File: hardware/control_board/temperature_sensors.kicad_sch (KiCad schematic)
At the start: 24 parts, among them J5 RTD, J5 TC, U2 MAX6675, U5 MCP6N11T-005E, U7 MCP6001T

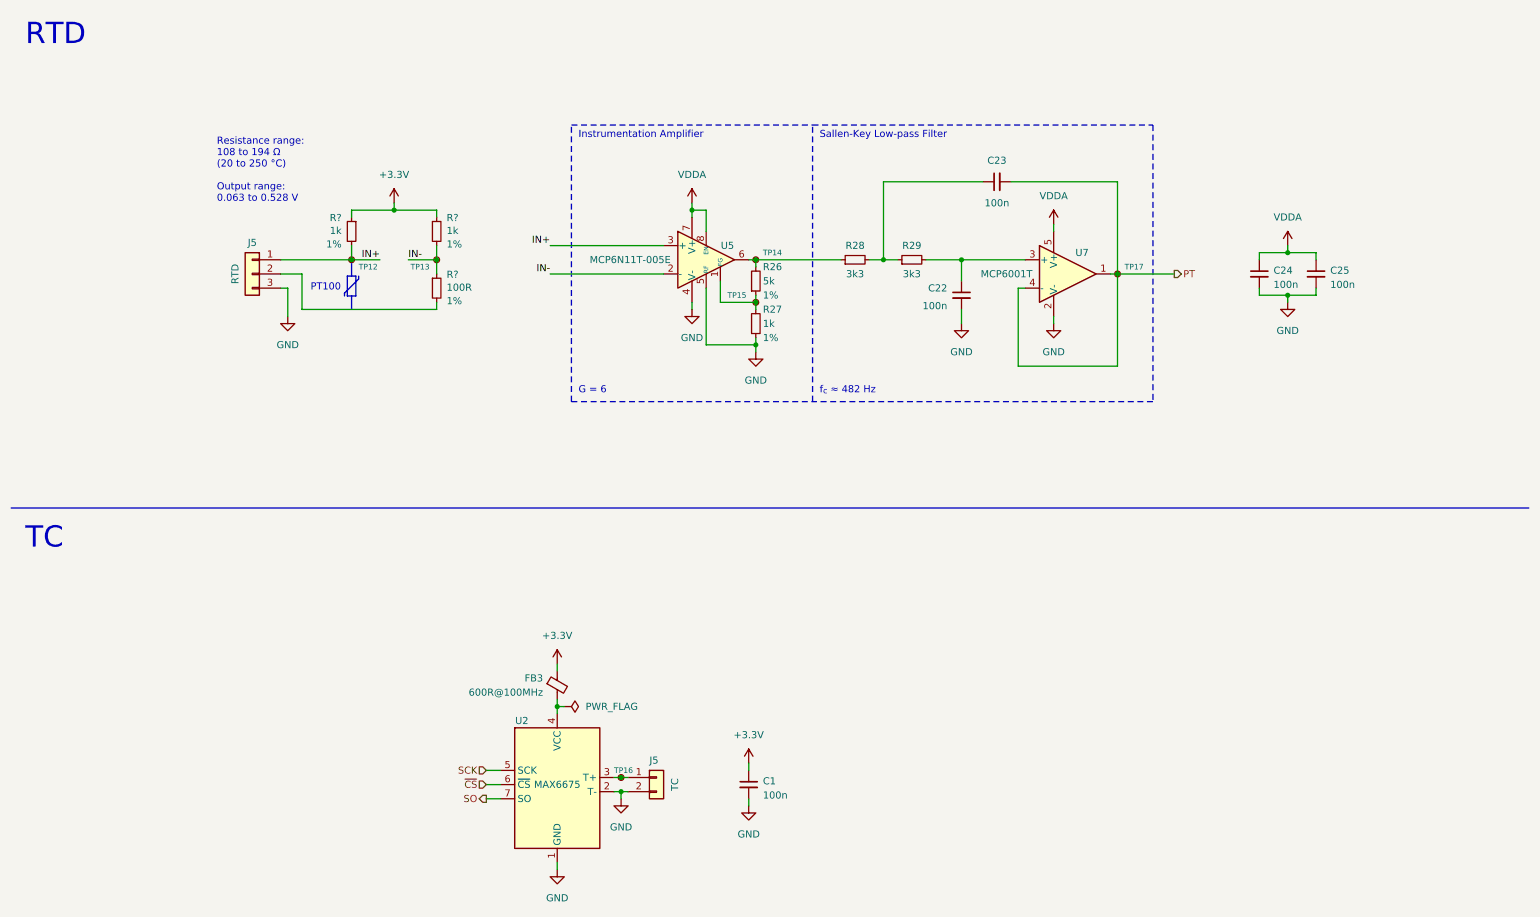
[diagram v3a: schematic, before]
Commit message: Place components on the control board PCB
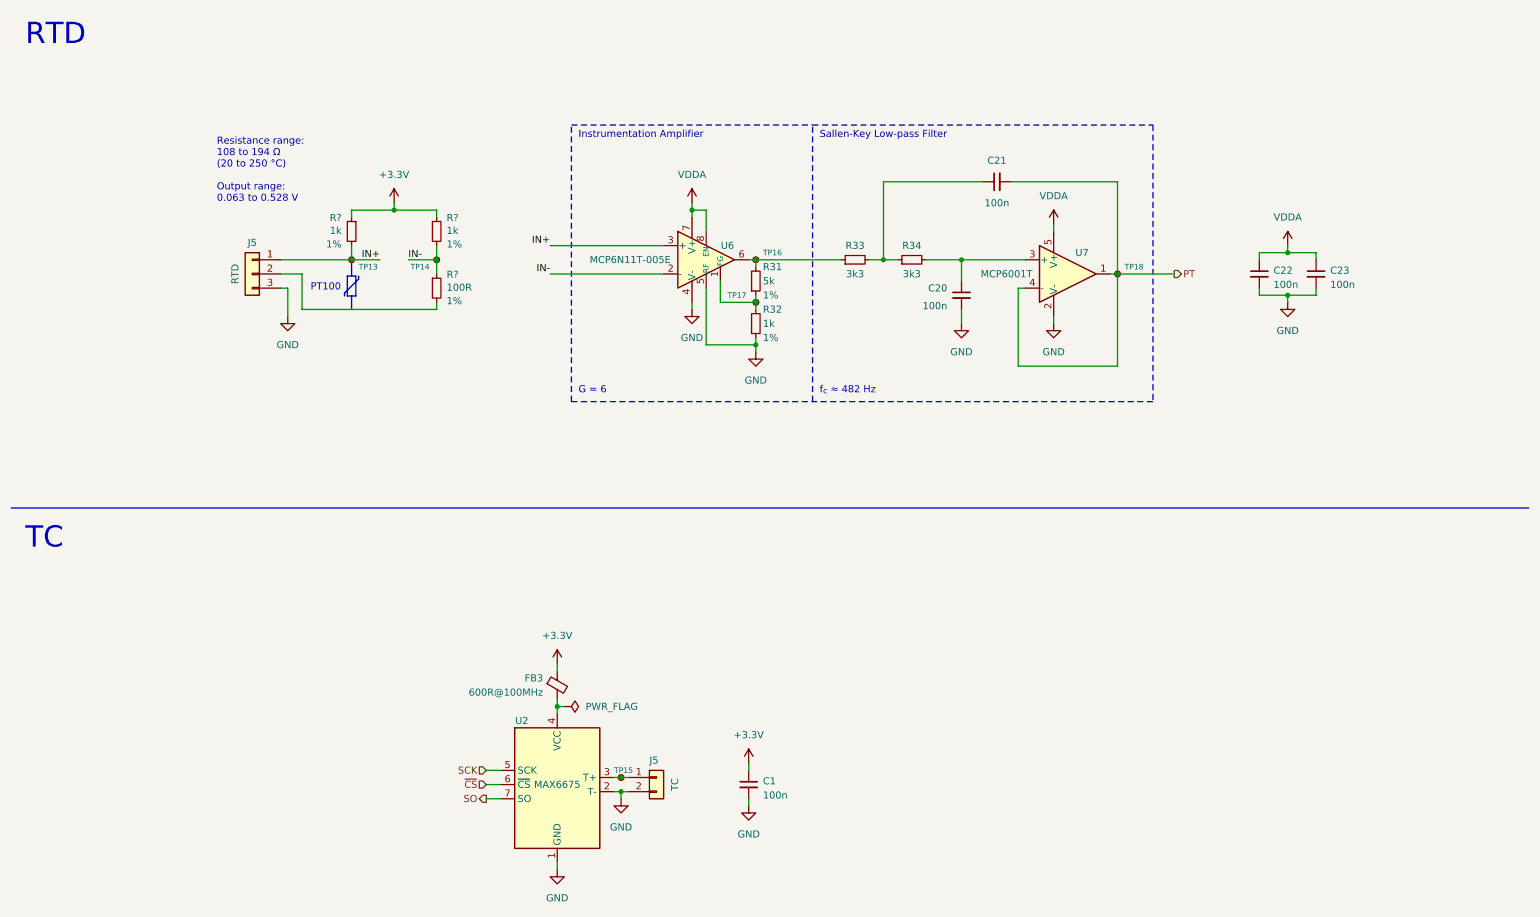
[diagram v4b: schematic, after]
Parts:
- renumbered C22 to C20, C23 to C21, C24 to C22, C25 to C23, R26 to R31, R27 to R32, R28 to R33, R29 to R34, TP12 to TP13, TP13 to TP14, TP16 to TP15, TP14 to TP16, TP15 to TP17, TP17 to TP18, U5 to U6
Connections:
- net GND: no longer U6.9 (EP)

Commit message: Route front panel PCB tracks
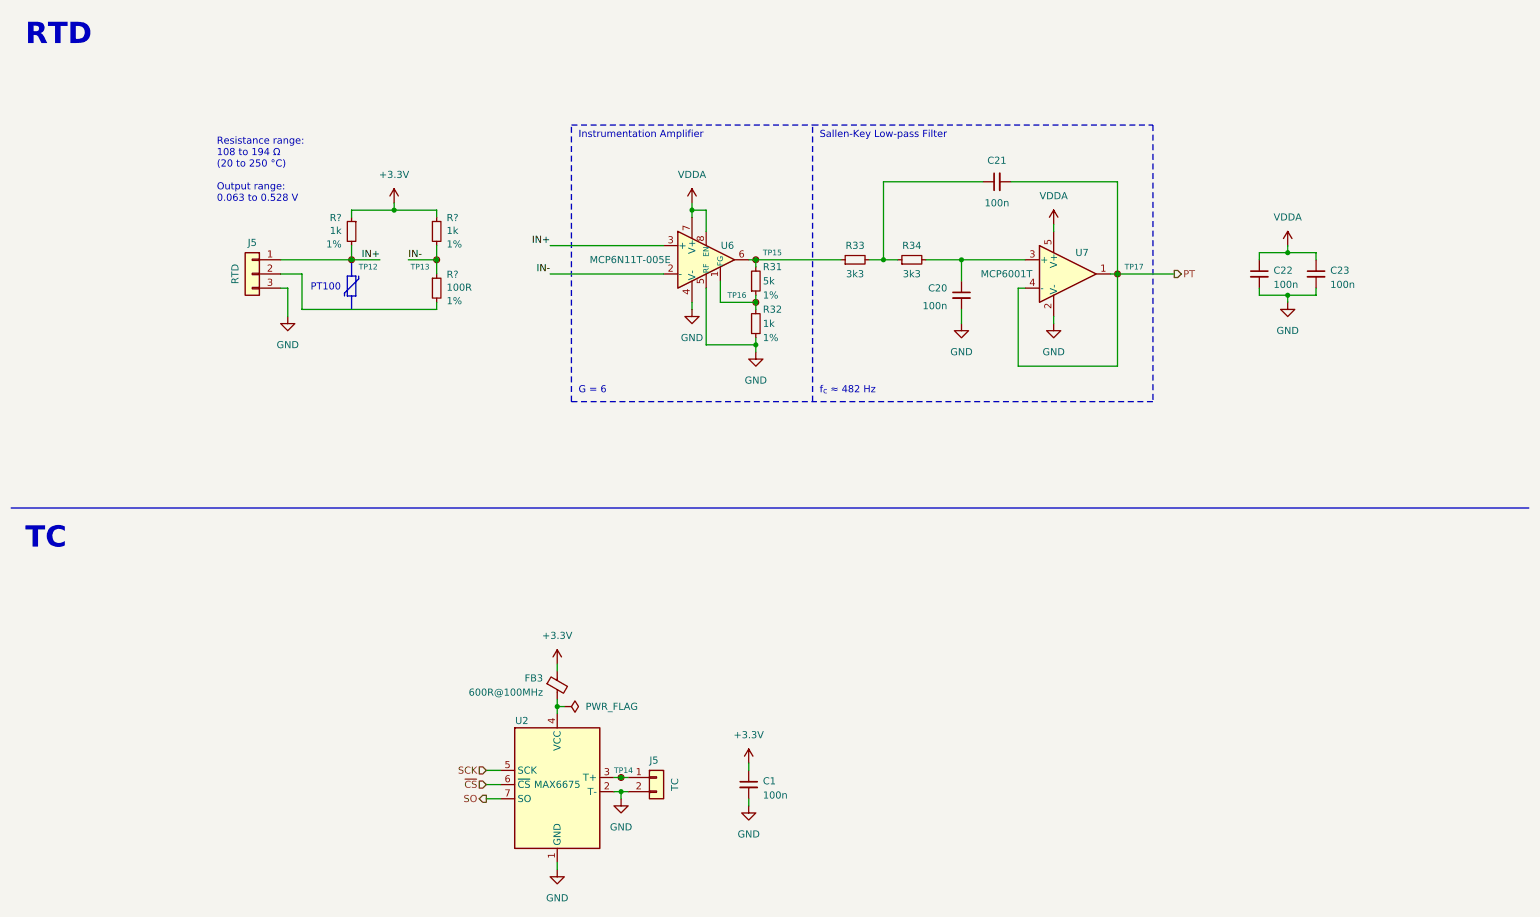
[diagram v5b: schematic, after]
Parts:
- TP12: renamed from TP13; now left out of the parts list
- TP13: renamed from TP14; now left out of the parts list
- TP14: renamed from TP15; now left out of the parts list
- TP15: renamed from TP16; now left out of the parts list
- TP16: renamed from TP17; now left out of the parts list
- TP17: renamed from TP18; now left out of the parts list
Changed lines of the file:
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@@
   )
   (text "TC" (at 15.24 110.49 0)
-    (effects (font (size 3.81 3.81)) (justify left bottom))
+    (effects (font (size 3.81 3.81) (thickness 0.762) bold) (justify left bottom))
   )
   (text "RTD" (at 15.24 20.32 0)
-    (effects (font (size 3.81 3.81)) (justify left bottom))
+    (effects (font (size 3.81 3.81) (thickness 0.762) bold) (justify left bottom))
   )
   (text "Sallen-Key Low-pass Filter" (at 157.48 36.83 0)
@@
   )
   (symbol (lib_id "Connector:TestPoint_Small") (at 210.82 60.96 0) (unit 1)
-    (in_bom yes) (on_board yes) (dnp no)
-    (property "Reference" "TP18" (at 212.09 59.69 0)
+    (in_bom no) (on_board yes) (dnp no)
+    (property "Reference" "TP17" (at 212.09 59.69 0)
       (effects (font (size 1 1)) (justify left))
     )
@@
       (project "control_board"
         (path "/b652b05a-4e3d-4ad1-b032-18886abe7d45/02711725-e382-48ba-bf33-23fe46c66e66"
-          (reference "TP18") (unit 1)
+          (reference "TP17") (unit 1)
         )
       )
@@
   )
   (symbol (lib_id "Connector:TestPoint_Small") (at 146.05 58.42 0) (unit 1)
-    (in_bom yes) (on_board yes) (dnp no)
-    (property "Reference" "TP16" (at 147.32 57.15 0)
+    (in_bom no) (on_board yes) (dnp no)
+    (property "Reference" "TP15" (at 147.32 57.15 0)
       (effects (font (size 1 1)) (justify left))
     )
@@
       (project "control_board"
         (path "/b652b05a-4e3d-4ad1-b032-18886abe7d45/02711725-e382-48ba-bf33-23fe46c66e66"
-          (reference "TP16") (unit 1)
+          (reference "TP15") (unit 1)
         )
       )
@@
   )
   (symbol (lib_id "Connector:TestPoint_Small") (at 146.05 66.04 0) (unit 1)
-    (in_bom yes) (on_board yes) (dnp no)
-    (property "Reference" "TP17" (at 140.97 64.77 0)
+    (in_bom no) (on_board yes) (dnp no)
+    (property "Reference" "TP16" (at 140.97 64.77 0)
       (effects (font (size 1 1)) (justify left))
     )
@@
       (project "control_board"
         (path "/b652b05a-4e3d-4ad1-b032-18886abe7d45/02711725-e382-48ba-bf33-23fe46c66e66"
-          (reference "TP17") (unit 1)
+          (reference "TP16") (unit 1)
         )
       )
@@
   )
   (symbol (lib_id "Connector:TestPoint_Small") (at 73.66 58.42 0) (unit 1)
-    (in_bom yes) (on_board yes) (dnp no)
-    (property "Reference" "TP13" (at 74.93 59.69 0)
+    (in_bom no) (on_board yes) (dnp no)
+    (property "Reference" "TP12" (at 74.93 59.69 0)
       (effects (font (size 1 1)) (justify left))
     )
@@
       (project "control_board"
         (path "/b652b05a-4e3d-4ad1-b032-18886abe7d45/02711725-e382-48ba-bf33-23fe46c66e66"
-          (reference "TP13") (unit 1)
+          (reference "TP12") (unit 1)
         )
       )
@@
   )
   (symbol (lib_id "Connector:TestPoint_Small") (at 121.92 151.13 180) (unit 1)
-    (in_bom yes) (on_board yes) (dnp no)
-    (property "Reference" "TP15" (at 120.65 149.86 0)
+    (in_bom no) (on_board yes) (dnp no)
+    (property "Reference" "TP14" (at 120.65 149.86 0)
       (effects (font (size 1 1)) (justify right))
     )
@@
       (project "control_board"
         (path "/b652b05a-4e3d-4ad1-b032-18886abe7d45/02711725-e382-48ba-bf33-23fe46c66e66"
-          (reference "TP15") (unit 1)
+          (reference "TP14") (unit 1)
         )
       )
@@
   )
   (symbol (lib_id "Connector:TestPoint_Small") (at 88.9 58.42 0) (unit 1)
-    (in_bom yes) (on_board yes) (dnp no)
-    (property "Reference" "TP14" (at 87.63 59.69 0)
+    (in_bom no) (on_board yes) (dnp no)
+    (property "Reference" "TP13" (at 87.63 59.69 0)
       (effects (font (size 1 1)) (justify right))
     )
@@
       (project "control_board"
         (path "/b652b05a-4e3d-4ad1-b032-18886abe7d45/02711725-e382-48ba-bf33-23fe46c66e66"
-          (reference "TP14") (unit 1)
-        )
-      )
+          (reference "TP13") (unit 1)
+        )
+      )

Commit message: Route control board PCB tracks
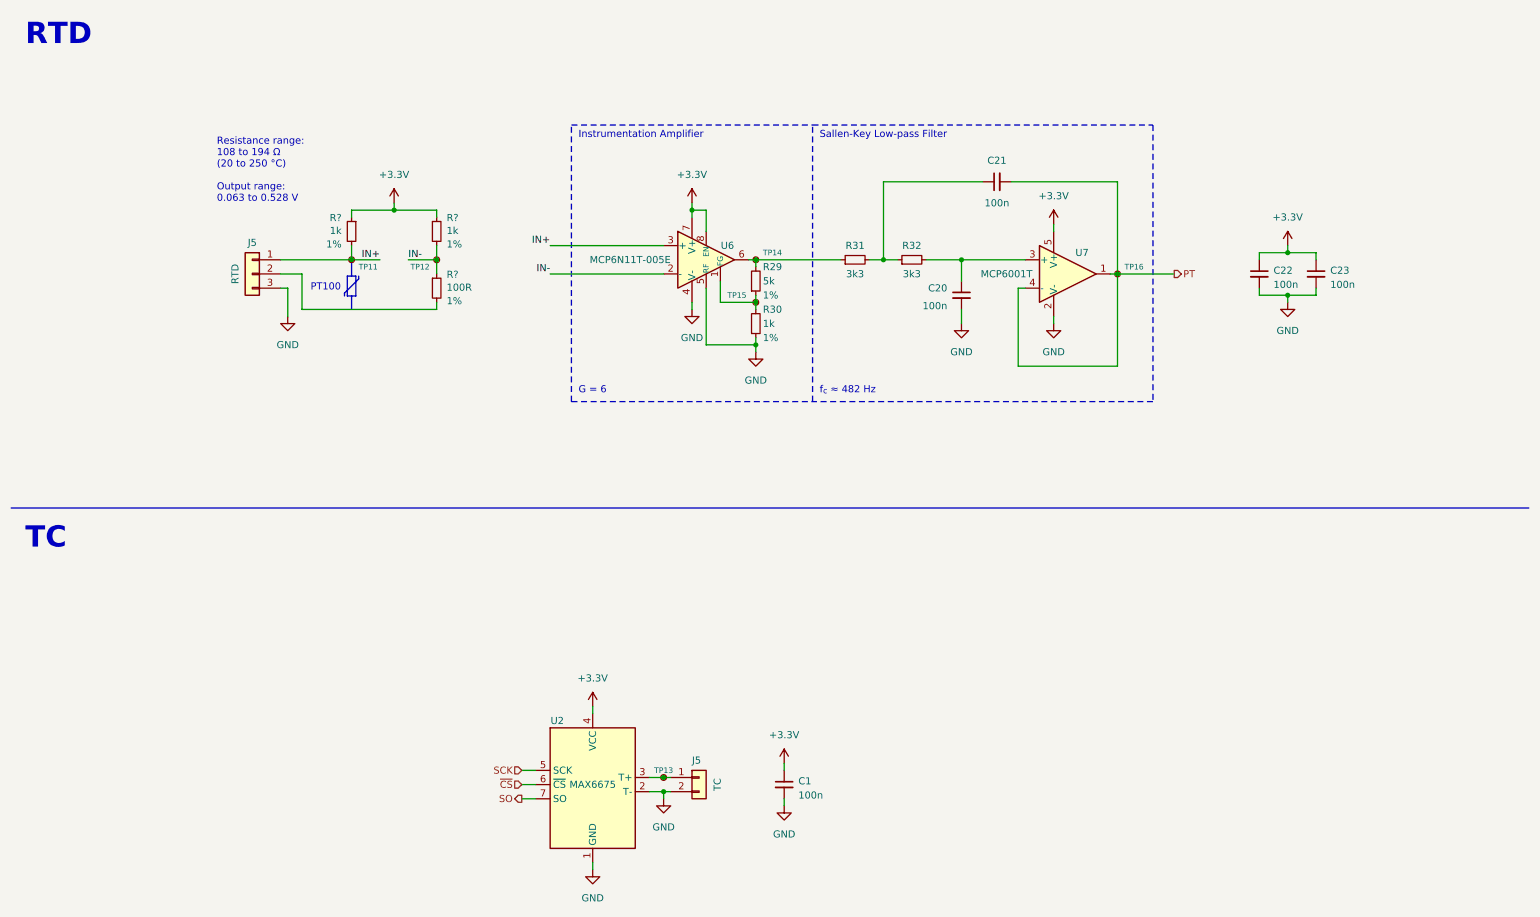
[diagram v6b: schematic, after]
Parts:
- removed FB3: 600R@100MHz, Inductor_SMD:L_0603_1608Metric, symbol Device:FerriteBead_Small
- renumbered R31 to R29, R32 to R30, R33 to R31, R34 to R32, TP12 to TP11, TP13 to TP12, TP14 to TP13, TP15 to TP14, TP16 to TP15, TP17 to TP16
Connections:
- net VDDA is gone; now on net +3.3V: C22.1, C23.1, U6.7 (V+), U6.8 (EN), U7.5 (V+)
- net +3.3V: now also U2.4 (VCC)
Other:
- moved on the sheet: C1, J5, TP13, U2

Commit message: Cleanup the project
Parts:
- R29: value 5k -> 4k99
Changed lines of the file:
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@@
       (effects (font (size 1.27 1.27)) (justify left))
     )
-    (property "Value" "5k" (at 147.32 62.23 0)
+    (property "Value" "4k99" (at 147.32 62.23 0)
       (effects (font (size 1.27 1.27)) (justify left))
     )
